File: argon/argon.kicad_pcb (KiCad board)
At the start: 2 copper layers, 60 x 50 mm, 78 parts, among them J1 USB, J2 V3V3-GND, J3 V3V3-GND, J4 V3V3-GND, J5 V3V3-GND, J6 V3V3-GND, J7 V3V3-GND, U1 LMC555xM, U2 AMS1117-3.3, U3 93LCxxA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

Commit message: USB design
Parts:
- R12, R13, U5: moved to F.Cu
- moved G*** 21.1 mm to (131.0, 93.0)
- moved R14 15.4 mm to (153.0, 91.2), turned to 270 degrees
- moved C19 13.6 mm to (140.0, 98.6), turned to 90 degrees
- moved C21 12.8 mm to (140.0, 103.2), turned to 90 degrees
- moved R12 12.2 mm to (151.3, 101.7), turned to 90 degrees
- moved R13 10.7 mm to (149.9, 101.7), turned to 90 degrees
- moved S3 10.0 mm to (125.1, 129.1)
- moved S4 10.0 mm to (157.1, 129.1)
- moved C16 10.0 mm to (150.0, 130.1)
- moved C17 10.0 mm to (170.4, 125.7)
- moved C18 10.0 mm to (150.0, 132.2)
- moved C20 10.0 mm to (150.0, 128.1)
- moved C23 10.0 mm to (150.0, 121.0)
- moved C3 10.0 mm to (141.0, 121.7)
- moved C6 10.0 mm to (141.0, 125.7)
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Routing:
- net V3V3: track 163.5 -> 131.2 mm
- net Net-(R13-Pad2): track 0.00 -> 8.54 mm
- net Net-(R12-Pad2): track 0.00 -> 8.44 mm
- net Net-(C10-Pad1): track 27.1 -> 19.9 mm
- net GND: track 0.00 -> 6.56 mm
- net Net-(R11-Pad2): track 5.32 -> 0.00 mm
- net Net-(R14-Pad2): track 4.41 -> 0.00 mm
- net Net-(J1-Pad2): track 0.00 -> 3.37 mm
- net Net-(J1-Pad3): track 0.00 -> 3.21 mm
- net Net-(R12-Pad1): track 4.79 -> 2.05 mm
- net Net-(C11-Pad1): track 28.3 -> 25.5 mm, vias 2 -> 1
- net Net-(R13-Pad1): track 4.39 -> 1.97 mm
- net LED_TX_B: track 0.00 -> 0.70 mm
- net VBUS: track 27.4 -> 26.9 mm
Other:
- board size 60 x 50 mm -> 60 x 60 mm

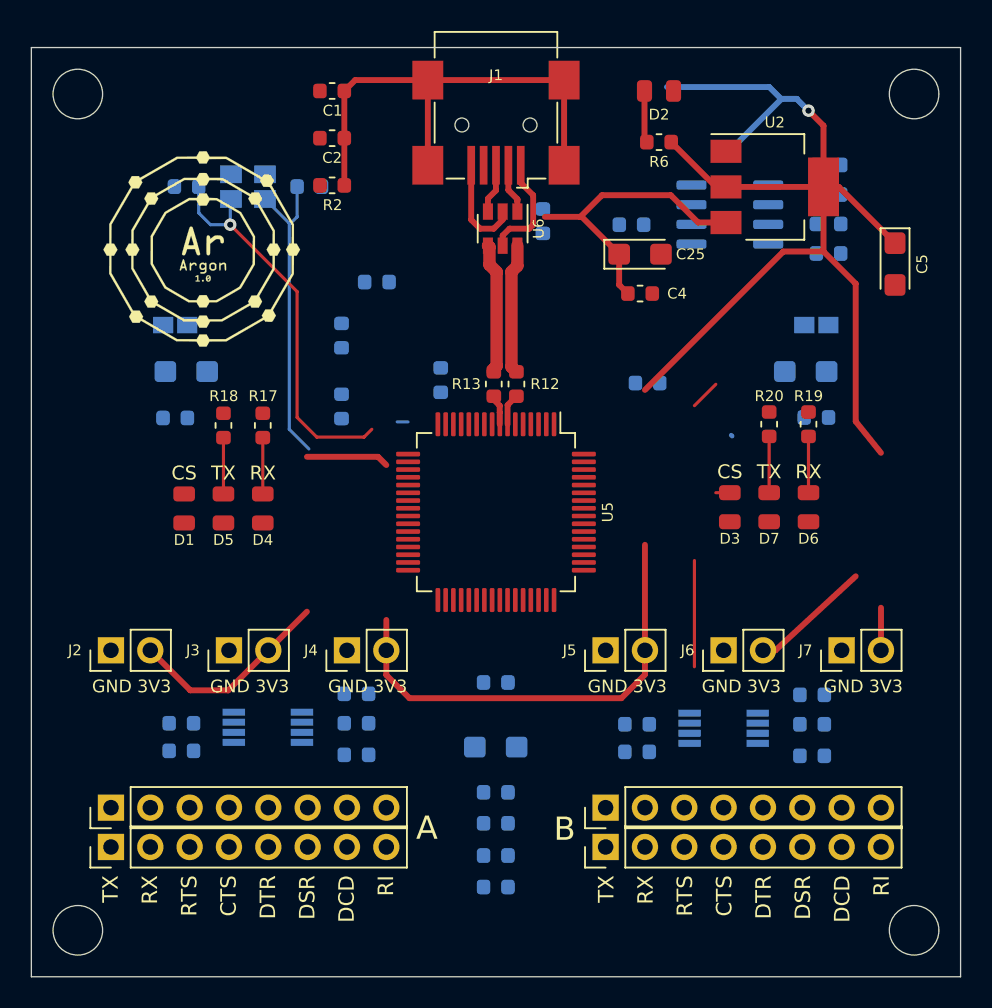
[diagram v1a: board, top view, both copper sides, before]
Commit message: Bigger logo & move resistors
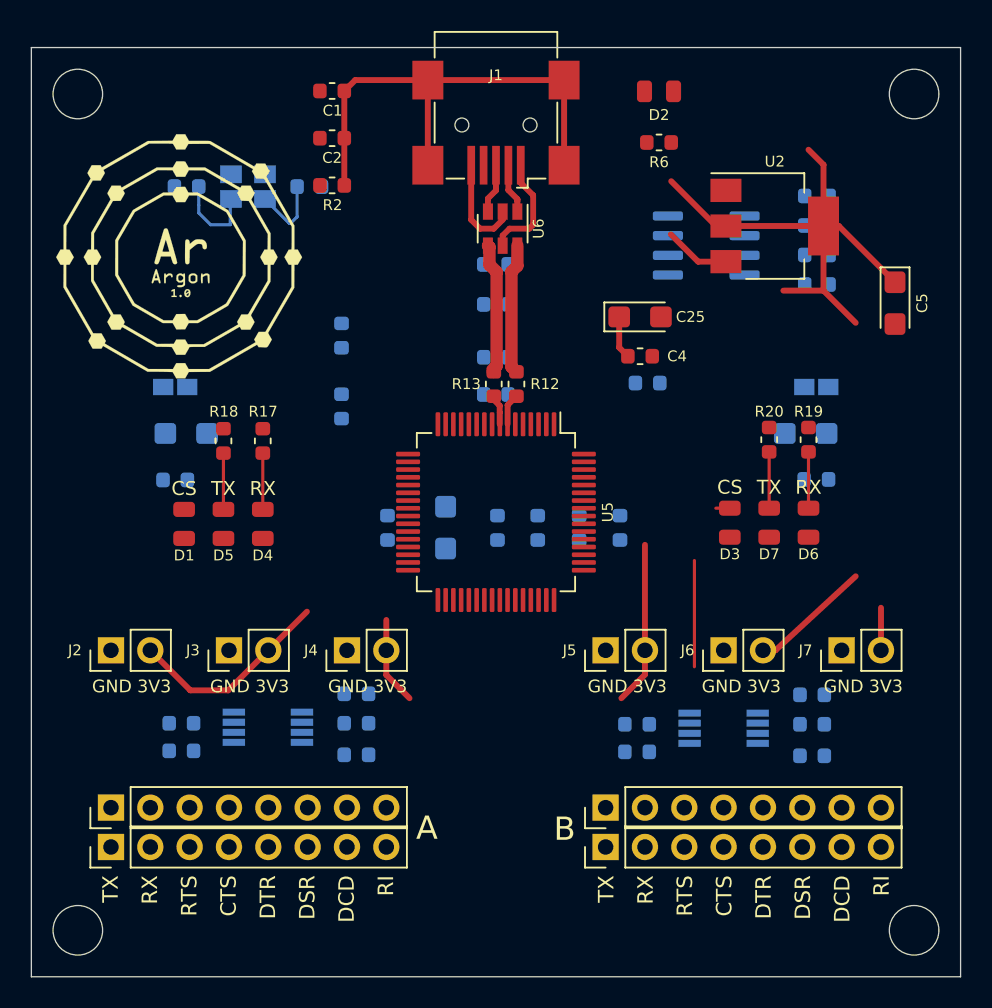
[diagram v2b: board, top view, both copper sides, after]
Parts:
- removed the G*** at (131.0, 93.0)
- added G***: LOGO, argon:argon_logo2, F.Cu at (129.5, 93.5)
- moved C8 24.5 mm to (158.0, 111.0), turned to 90 degrees
- moved C18 21.8 mm to (155.4, 111.0), turned to 90 degrees
- moved C16 19.3 mm to (152.7, 111.0), turned to 90 degrees
- moved C20 17.1 mm to (150.1, 111.0), turned to 90 degrees
- moved C7 14.5 mm to (146.8, 111.0), turned to 270 degrees
- moved C24 14.0 mm to (150.0, 102.4), turned to 180 degrees
- moved C23 12.2 mm to (143.0, 111.0), turned to 270 degrees
- moved C5 9.10 mm to (150.0, 100.0)
- moved R11 6.05 mm to (150.0, 96.6), turned to 0 degrees
- moved R14 4.11 mm to (150.0, 94.0), turned to 0 degrees
- moved C25 4.05 mm to (159.3, 97.4)
- moved C4 4.05 mm to (159.3, 99.9)
- moved C12 4.00 mm to (170.0, 104.9)
- moved C13 4.00 mm to (130.0, 104.9)
- moved C14 4.00 mm to (170.7, 107.9)
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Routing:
- net V3V3: track 131.2 -> 72.9 mm, vias 1 -> 0
- net Net-(C11-Pad1): track 25.5 -> 5.72 mm, vias 1 -> 0
- net Net-(C10-Pad1): track 19.9 -> 4.85 mm
- net VBUS: track 26.9 -> 14.7 mm
- net Net-(D2-Pad2): track 3.36 -> 0.00 mm
- net Net-(D3-Pad2): track 9.72 -> 7.76 mm
- net LED_TX_B: track 0.70 -> 0.00 mm

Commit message: 555 routes
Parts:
- moved C3 2.48 mm to (138.5, 121.7)
- moved C6 2.48 mm to (138.5, 125.7)
- moved R3 2.48 mm to (138.5, 123.6)
- moved R1 2.48 mm to (127.2, 125.4)
- moved R4 2.48 mm to (127.2, 123.6)
- moved U1 2.48 mm to (132.8, 123.9)
- turned R15 to 180 degrees
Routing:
- net V3V3: track 72.9 -> 97.6 mm
- net Net-(D1-Pad2): track 0.00 -> 21.0 mm, vias 0 -> 1
- net Net-(D3-Pad2): track 7.76 -> 22.9 mm, vias 0 -> 1
- net CS_B: track 0.00 -> 9.32 mm
- net CS_A: track 0.00 -> 8.45 mm
- net Net-(C17-Pad1): track 0.00 -> 5.67 mm
- net Net-(C6-Pad1): track 0.00 -> 5.02 mm
- net Net-(C3-Pad1): track 0.00 -> 3.22 mm
- net Net-(C9-Pad1): track 0.00 -> 3.22 mm
- net Net-(R16-Pad2): track 0.00 -> 2.63 mm
- net Net-(R4-Pad2): track 0.00 -> 2.53 mm

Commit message: FBs routing
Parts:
- removed the C5 at (150.0, 100.0)
- moved C14 41.6 mm to (129.1, 107.9), turned to 0 degrees
- moved C15 41.6 mm to (170.9, 107.9), turned to 180 degrees
- moved C12 40.2 mm to (129.8, 104.9), turned to 180 degrees
- moved C13 40.2 mm to (170.2, 104.9), turned to 0 degrees
- moved C24 13.4 mm to (157.0, 90.9), turned to 0 degrees
- moved R14 4.87 mm to (150.6, 98.8), turned to 180 degrees
- moved R11 4.29 mm to (150.6, 100.8)
- moved C11 4.00 mm to (128.8, 92.8)
- moved Y1 4.00 mm to (132.8, 92.8)
- moved C10 4.00 mm to (136.7, 92.8)
- moved C21 2.72 mm to (140.0, 105.9)
- moved C19 0.97 mm to (140.0, 99.6)
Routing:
- net Net-(C12-Pad1): track 0.00 -> 30.3 mm, vias 0 -> 1
- net Net-(C13-Pad1): track 0.00 -> 28.4 mm, vias 0 -> 1
- net VBUS: track 14.7 -> 29.4 mm
- net Net-(R11-Pad2): track 0.00 -> 12.8 mm, vias 0 -> 1
- net Net-(R14-Pad2): track 0.00 -> 7.79 mm, vias 0 -> 1
- net V3V3: track 97.6 -> 103.4 mm, vias 0 -> 1
- net Net-(D2-Pad2): track 0.00 -> 3.36 mm
- net (no net): track 0.00 -> 1.27 mm
- net Net-(C11-Pad1): track 5.72 -> 4.45 mm

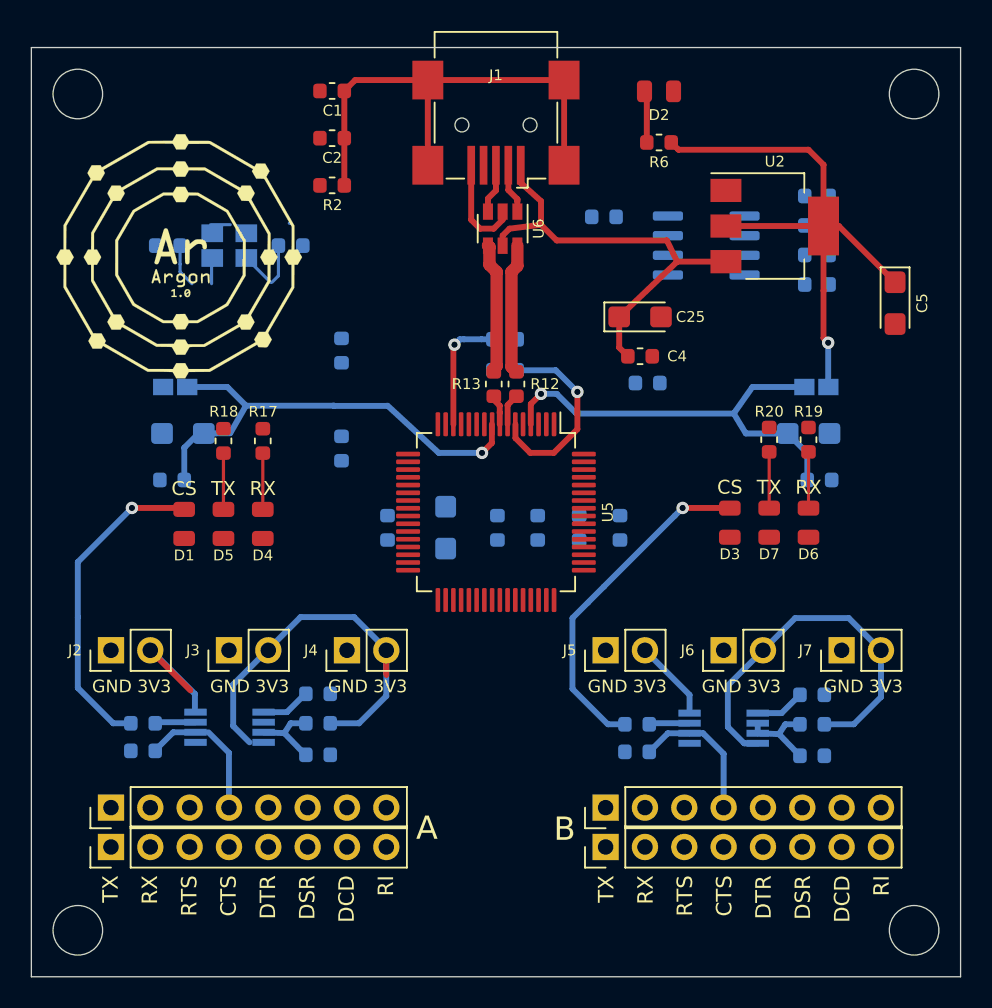
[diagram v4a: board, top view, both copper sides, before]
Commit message: TX & RX leds and A pads
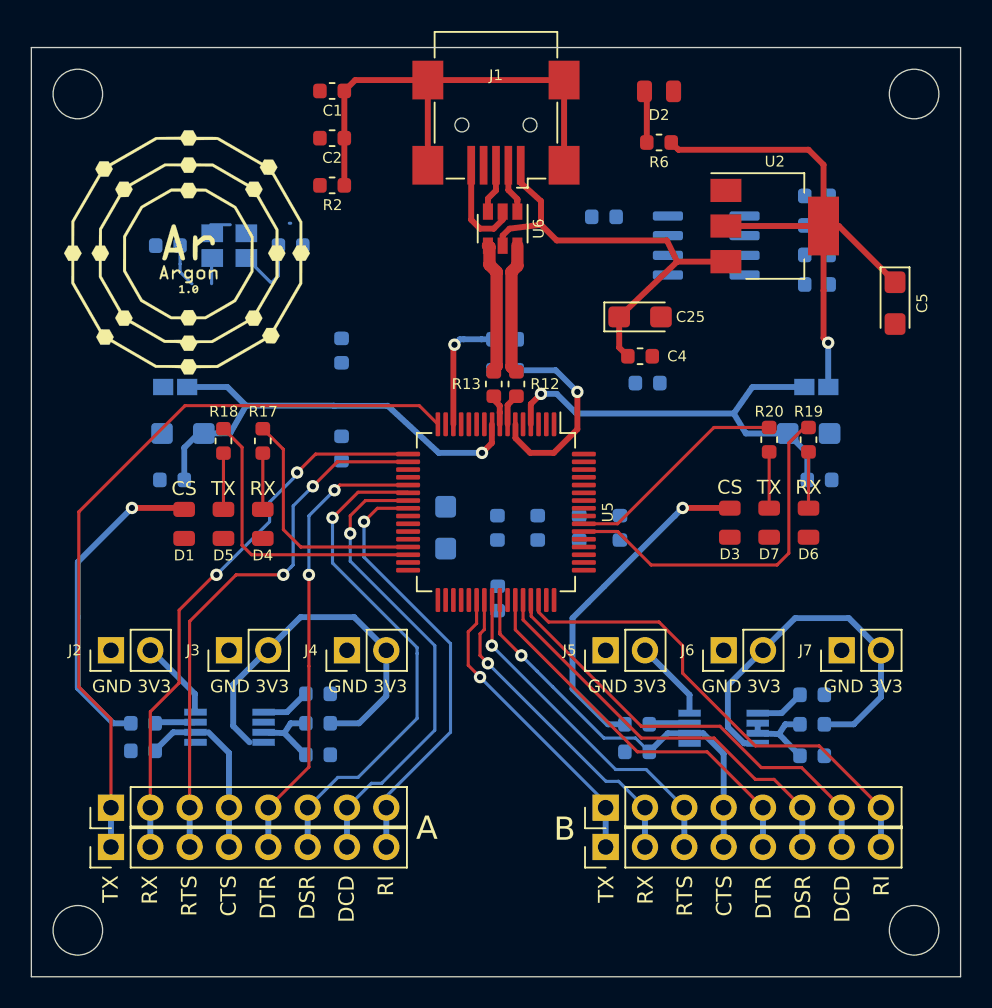
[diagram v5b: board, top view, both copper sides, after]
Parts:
- moved C23 8.45 mm to (150.1, 115.6)
- moved G*** 0.57 mm to (130.0, 93.2)
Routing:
- net Net-(S1-Pad1): track 0.00 -> 49.0 mm
- net Net-(S1-Pad2): track 0.00 -> 35.8 mm, vias 0 -> 2
- net Net-(S1-Pad3): track 0.00 -> 35.2 mm, vias 0 -> 2
- net Net-(S1-Pad6): track 0.00 -> 32.8 mm, vias 0 -> 1
- net Net-(S2-Pad8): track 0.00 -> 31.7 mm
- net Net-(S1-Pad7): track 0.00 -> 30.5 mm, vias 0 -> 1
- net Net-(S1-Pad5): track 0.00 -> 29.7 mm, vias 0 -> 2
- net Net-(S2-Pad7): track 0.00 -> 28.8 mm
- net Net-(S1-Pad8): track 0.00 -> 28.4 mm, vias 0 -> 1
- net Net-(S2-Pad6): track 0.00 -> 26.9 mm
- net Net-(S2-Pad5): track 0.00 -> 25.2 mm
- net LED_RX_B: track 0.27 -> 23.5 mm
- net Net-(S2-Pad3): track 0.00 -> 22.3 mm, vias 0 -> 1
- net Net-(S2-Pad2): track 0.00 -> 21.0 mm, vias 0 -> 1
- net Net-(S2-Pad1): track 0.00 -> 19.8 mm, vias 0 -> 1
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
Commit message: V1.8 & V3.3
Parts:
- C22: moved to F.Cu
- moved C22 22.8 mm to (141.5, 115.3), turned to 0 degrees
- moved C7 20.3 mm to (167.1, 112.0), turned to 90 degrees
- moved C21 13.4 mm to (152.0, 111.8), turned to 270 degrees
- moved C16 13.0 mm to (144.6, 100.8), turned to 0 degrees
- moved C19 12.2 mm to (148.2, 108.6)
- moved C23 12.0 mm to (159.0, 107.4)
- moved C8 6.76 mm to (164.6, 112.5), turned to 270 degrees
- moved C18 4.16 mm to (152.0, 108.6)
- moved C20 2.03 mm to (148.2, 111.8), turned to 270 degrees
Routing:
- net VCORE: track 0.00 -> 63.0 mm, vias 0 -> 4
- net V3V3: track 98.2 -> 136.6 mm, vias 1 -> 6

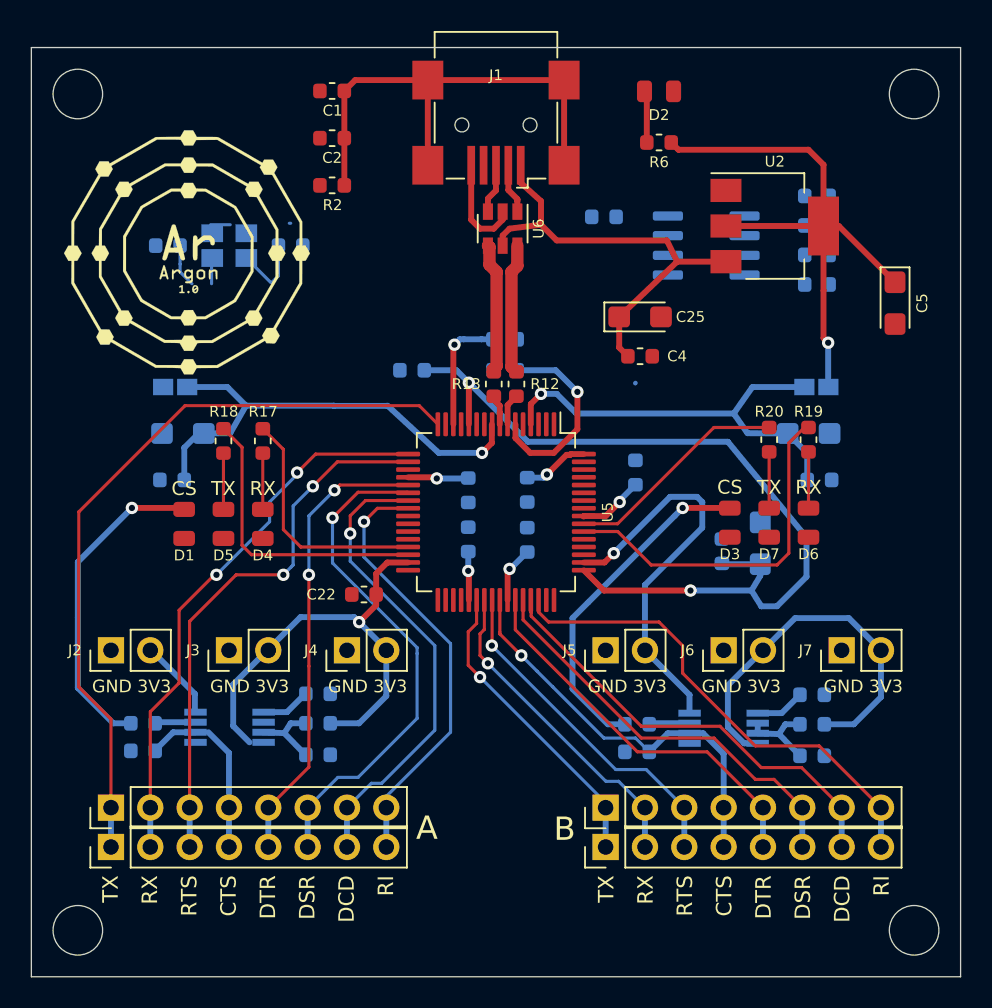
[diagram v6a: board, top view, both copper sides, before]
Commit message: Move all up to avoid holes overlapping
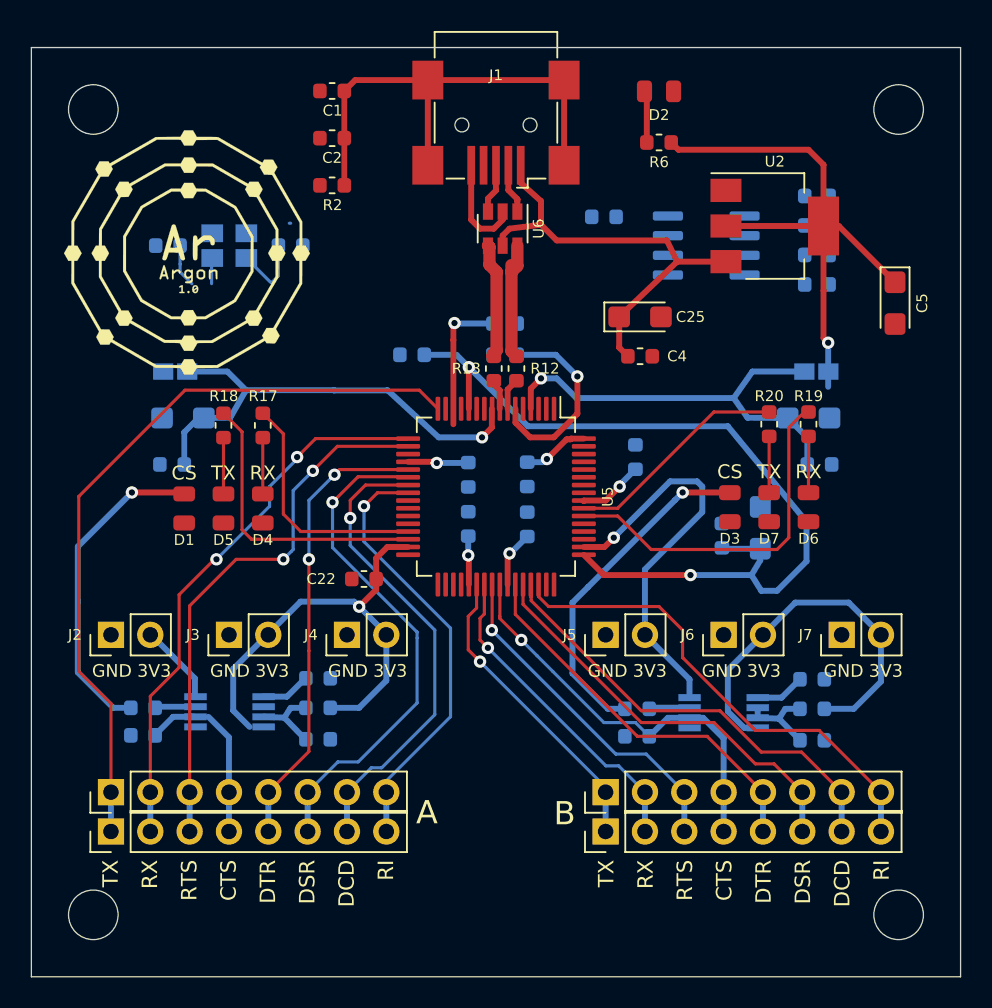
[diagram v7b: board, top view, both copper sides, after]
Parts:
- moved H1 1.41 mm to (124.0, 84.0)
- moved H2 1.41 mm to (176.0, 84.0)
- moved H3 1.41 mm to (124.0, 136.0)
- moved H4 1.41 mm to (176.0, 136.0)
- moved R14 1.02 mm to (150.6, 97.8)
- moved C12 1.00 mm to (129.8, 103.9)
- moved C13 1.00 mm to (170.2, 103.9)
- moved C14 1.00 mm to (129.1, 106.9)
- moved C15 1.00 mm to (170.9, 106.9)
- moved C16 1.00 mm to (144.6, 99.8)
- moved C17 1.00 mm to (170.4, 124.7)
- moved C18 1.00 mm to (152.0, 107.6)
- moved C19 1.00 mm to (148.2, 107.6)
- moved C20 1.00 mm to (148.2, 110.8)
- moved C21 1.00 mm to (152.0, 110.8)
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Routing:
- net (no net): track 1.27 -> 0.00 mm
- net Net-(R14-Pad2): track 7.79 -> 9.05 mm
- net Net-(R13-Pad2): track 8.54 -> 7.54 mm
- net Net-(R12-Pad2): track 8.44 -> 7.82 mm
